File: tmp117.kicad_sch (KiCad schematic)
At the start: 12 parts, among them U6 MCP9804_MSOP, U7 M24C02-WMN

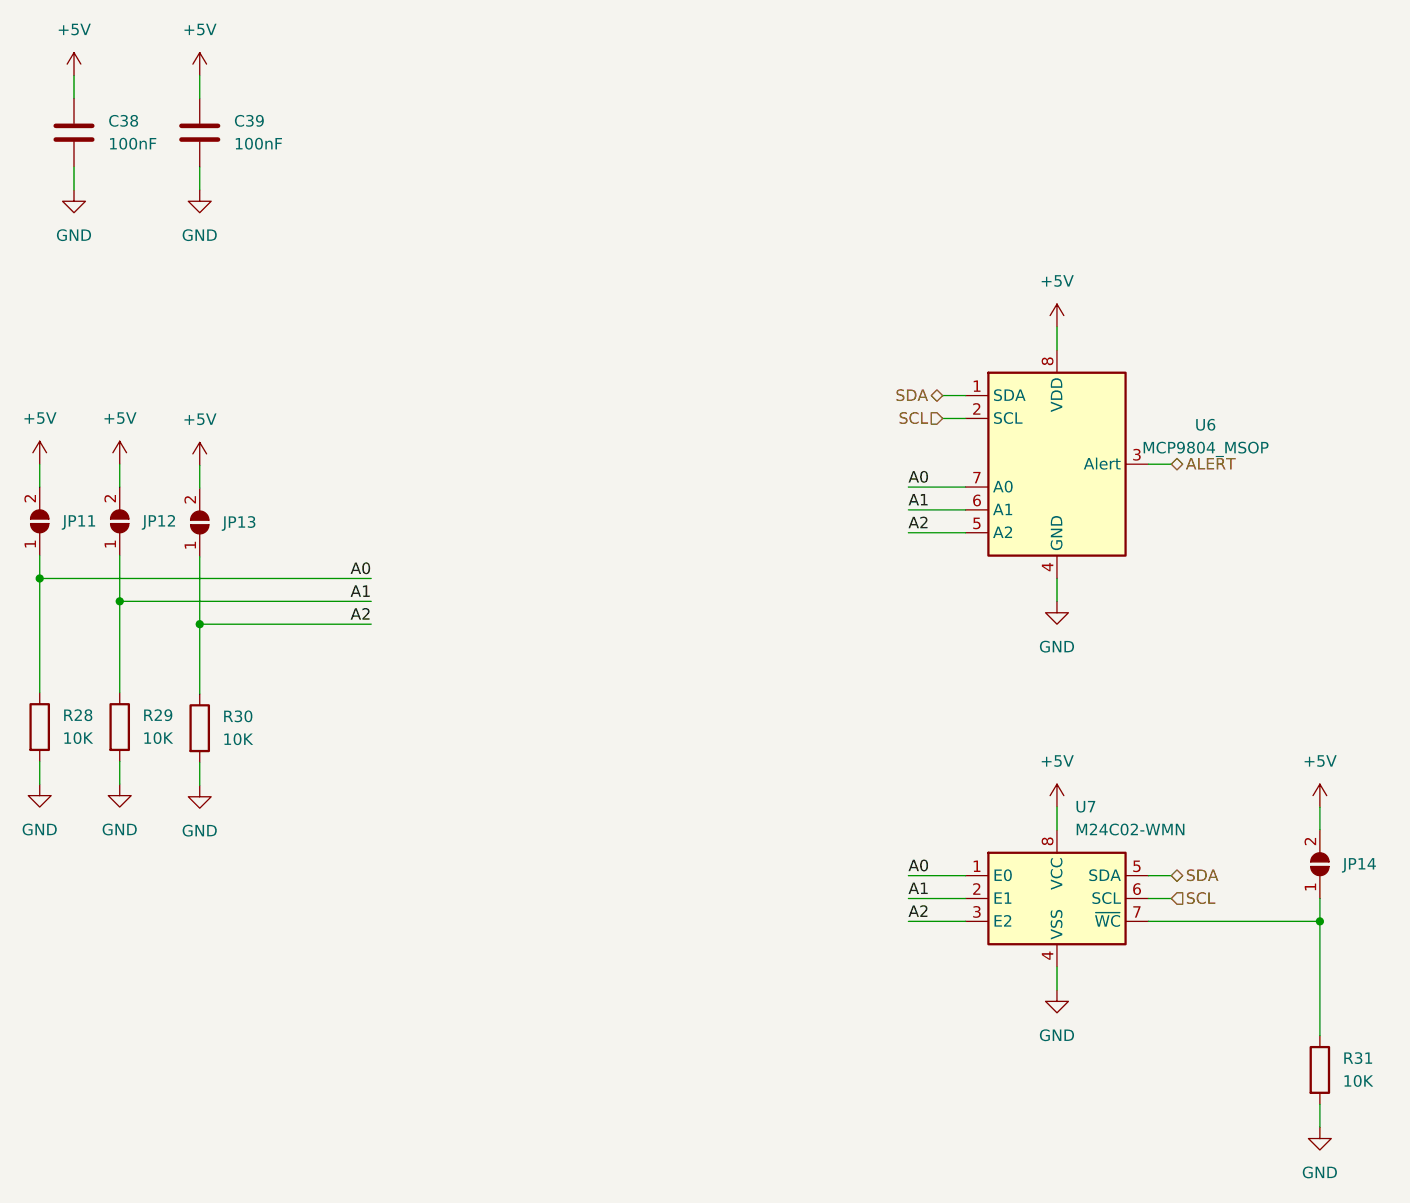
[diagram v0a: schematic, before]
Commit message: Add a lot of nice to haves
* Jumpers to bridge isolation
* I2C pullups with jumpers for input
* Labels on input connectors
* Geographic reference counts
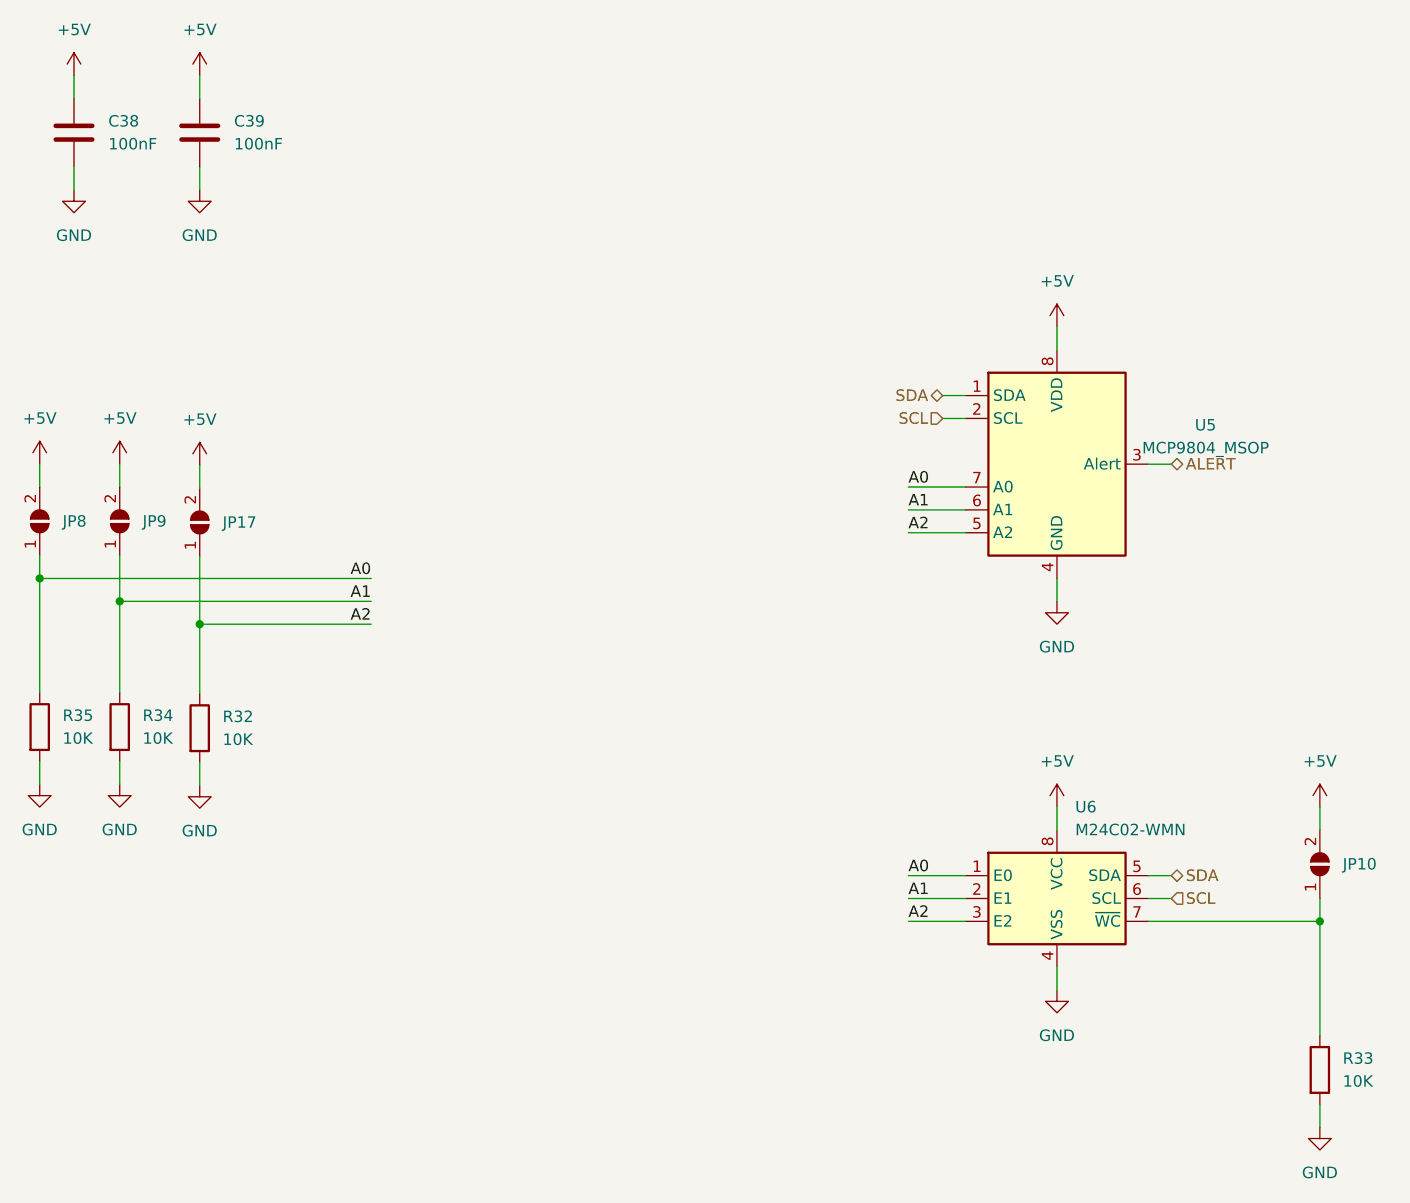
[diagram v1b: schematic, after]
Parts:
- renumbered JP14 to JP10, JP13 to JP17, JP11 to JP8, JP12 to JP9, R30 to R32, R31 to R33, R29 to R34, R28 to R35, U6 to U5, U7 to U6
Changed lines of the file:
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@@
   (symbol (lib_id "Sensor_Temperature:MCP9804_MSOP") (at 151.13 69.85 0) (unit 1)
     (in_bom yes) (on_board yes) (fields_autoplaced)
-    (property "Reference" "U6" (id 0) (at 167.64 65.5193 0))
+    (property "Reference" "U5" (id 0) (at 167.64 65.5193 0))
     (property "Value" "MCP9804_MSOP" (id 1) (at 167.64 68.0593 0))
     (property "Footprint" "Package_SO:MSOP-8_3x3mm_P0.65mm" (id 2) (at 151.13 69.85 0)
@@
   (symbol (lib_id "Jumper:SolderJumper_2_Open") (at 38.1 76.2 90) (unit 1)
     (in_bom yes) (on_board yes) (fields_autoplaced)
-    (property "Reference" "JP11" (id 0) (at 40.64 76.1999 90)
+    (property "Reference" "JP8" (id 0) (at 40.64 76.1999 90)
       (effects (font (size 1.27 1.27)) (justify right))
     )
@@
   (symbol (lib_id "Jumper:SolderJumper_2_Open") (at 55.88 76.3265 90) (unit 1)
     (in_bom yes) (on_board yes) (fields_autoplaced)
-    (property "Reference" "JP13" (id 0) (at 58.42 76.3264 90)
+    (property "Reference" "JP17" (id 0) (at 58.42 76.3264 90)
       (effects (font (size 1.27 1.27)) (justify right))
     )
@@
   (symbol (lib_id "Device:R") (at 180.34 137.16 0) (unit 1)
     (in_bom yes) (on_board yes) (fields_autoplaced)
-    (property "Reference" "R31" (id 0) (at 182.88 135.8899 0)
+    (property "Reference" "R33" (id 0) (at 182.88 135.8899 0)
       (effects (font (size 1.27 1.27)) (justify left))
     )
@@
   (symbol (lib_id "Jumper:SolderJumper_2_Open") (at 180.34 114.3 90) (unit 1)
     (in_bom yes) (on_board yes) (fields_autoplaced)
-    (property "Reference" "JP14" (id 0) (at 182.88 114.2999 90)
+    (property "Reference" "JP10" (id 0) (at 182.88 114.2999 90)
       (effects (font (size 1.27 1.27)) (justify right))
     )
@@
   (symbol (lib_id "Memory_EEPROM:M24C02-WMN") (at 151.13 118.11 0) (unit 1)
     (in_bom yes) (on_board yes) (fields_autoplaced)
-    (property "Reference" "U7" (id 0) (at 153.1494 107.95 0)
+    (property "Reference" "U6" (id 0) (at 153.1494 107.95 0)
       (effects (font (size 1.27 1.27)) (justify left))
     )
@@
   (symbol (lib_id "Device:R") (at 55.88 99.1865 0) (unit 1)
     (in_bom yes) (on_board yes) (fields_autoplaced)
-    (property "Reference" "R30" (id 0) (at 58.42 97.9164 0)
+    (property "Reference" "R32" (id 0) (at 58.42 97.9164 0)
       (effects (font (size 1.27 1.27)) (justify left))
     )
@@
   (symbol (lib_id "Jumper:SolderJumper_2_Open") (at 46.99 76.2 90) (unit 1)
     (in_bom yes) (on_board yes) (fields_autoplaced)
-    (property "Reference" "JP12" (id 0) (at 49.53 76.1999 90)
+    (property "Reference" "JP9" (id 0) (at 49.53 76.1999 90)
       (effects (font (size 1.27 1.27)) (justify right))
     )
@@
   (symbol (lib_id "Device:R") (at 46.99 99.06 0) (unit 1)
     (in_bom yes) (on_board yes) (fields_autoplaced)
-    (property "Reference" "R29" (id 0) (at 49.53 97.7899 0)
+    (property "Reference" "R34" (id 0) (at 49.53 97.7899 0)
       (effects (font (size 1.27 1.27)) (justify left))
     )
@@
   (symbol (lib_id "Device:R") (at 38.1 99.06 0) (unit 1)
     (in_bom yes) (on_board yes) (fields_autoplaced)
-    (property "Reference" "R28" (id 0) (at 40.64 97.7899 0)
-      (effects (font (size 1.27 1.27)) (justify left))
-    )
+    (property "Reference" "R35" (id 0) (at 40.64 97.7899 0)
+      (effects (font (size 1.27 1.27)) (justify left))
+    )
